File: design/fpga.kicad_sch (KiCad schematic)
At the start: 80 parts, among them J7 DEBUG_FPGA_GPIO, J8 DIGILENT_JTAG_HS2_01X06, SW1 RST, SW2 PROG, U13 XC7S15-FTGB196, U14 IS25LP064A-JKx

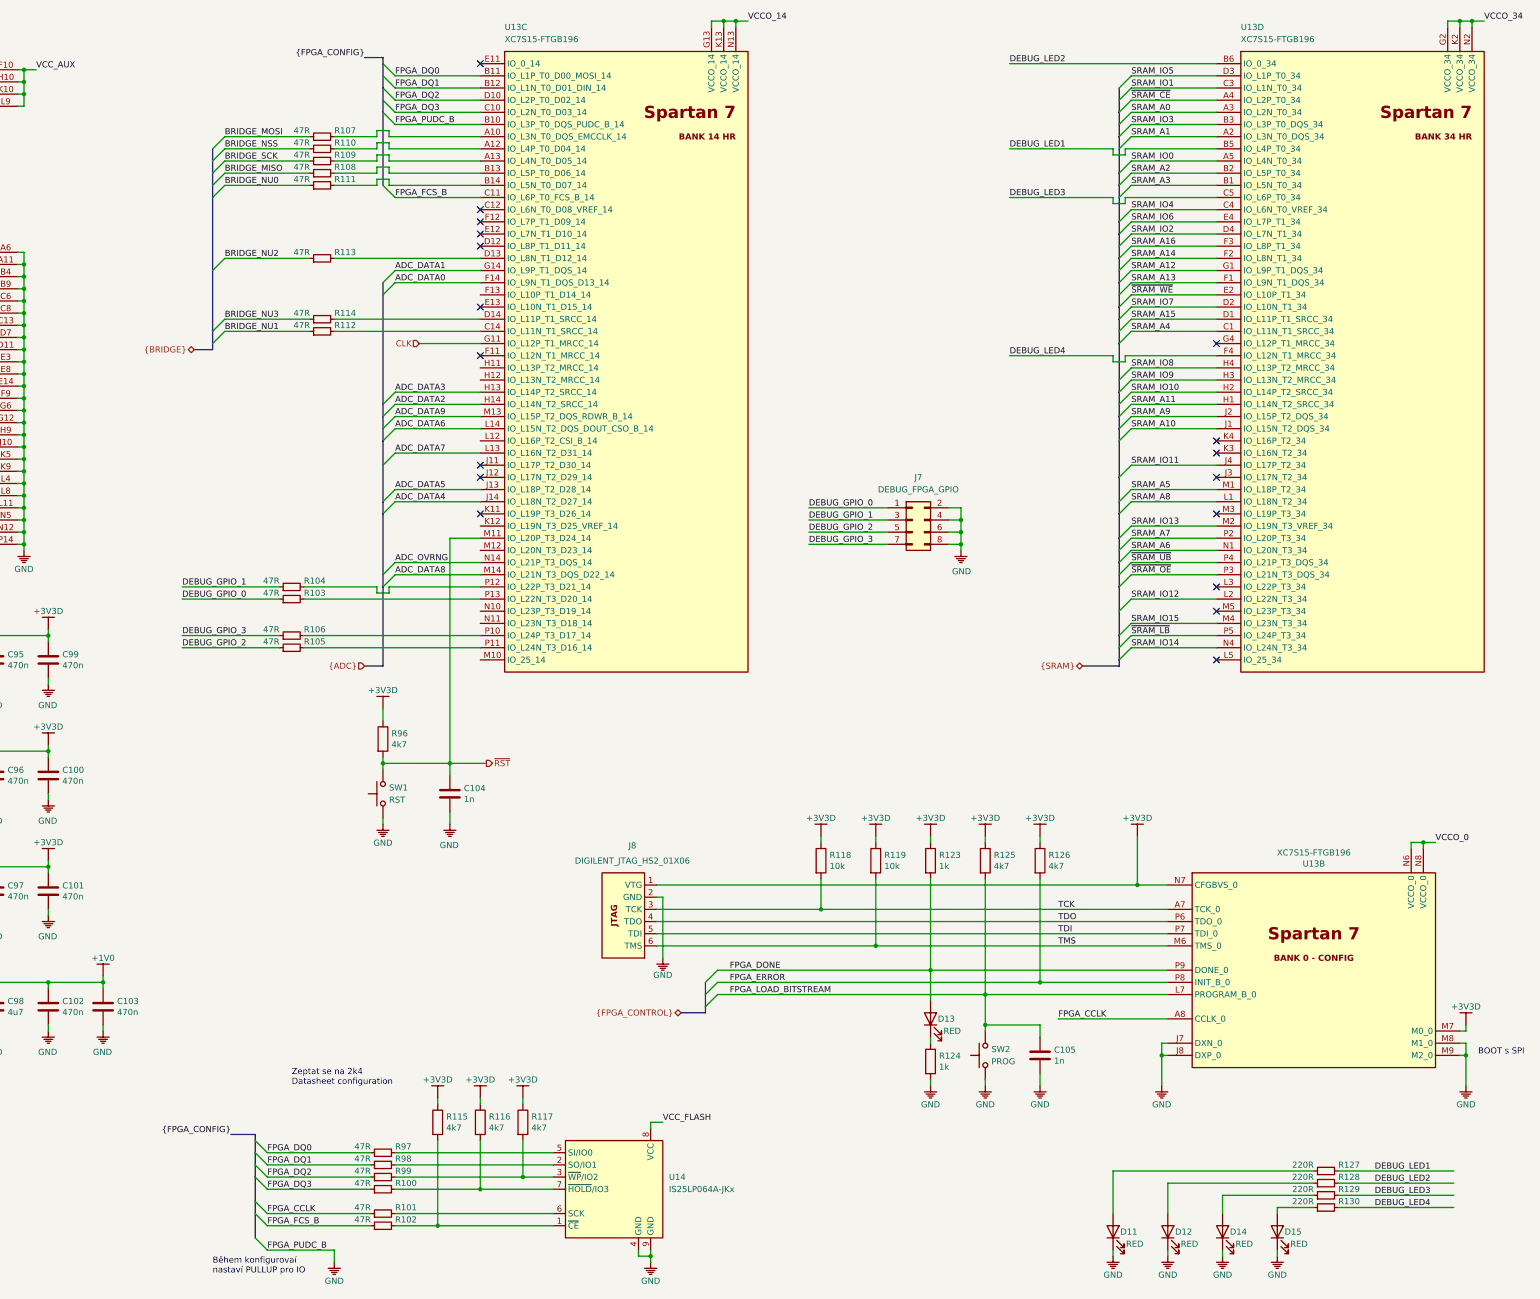
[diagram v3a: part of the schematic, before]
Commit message: Refactored FPGA schematic
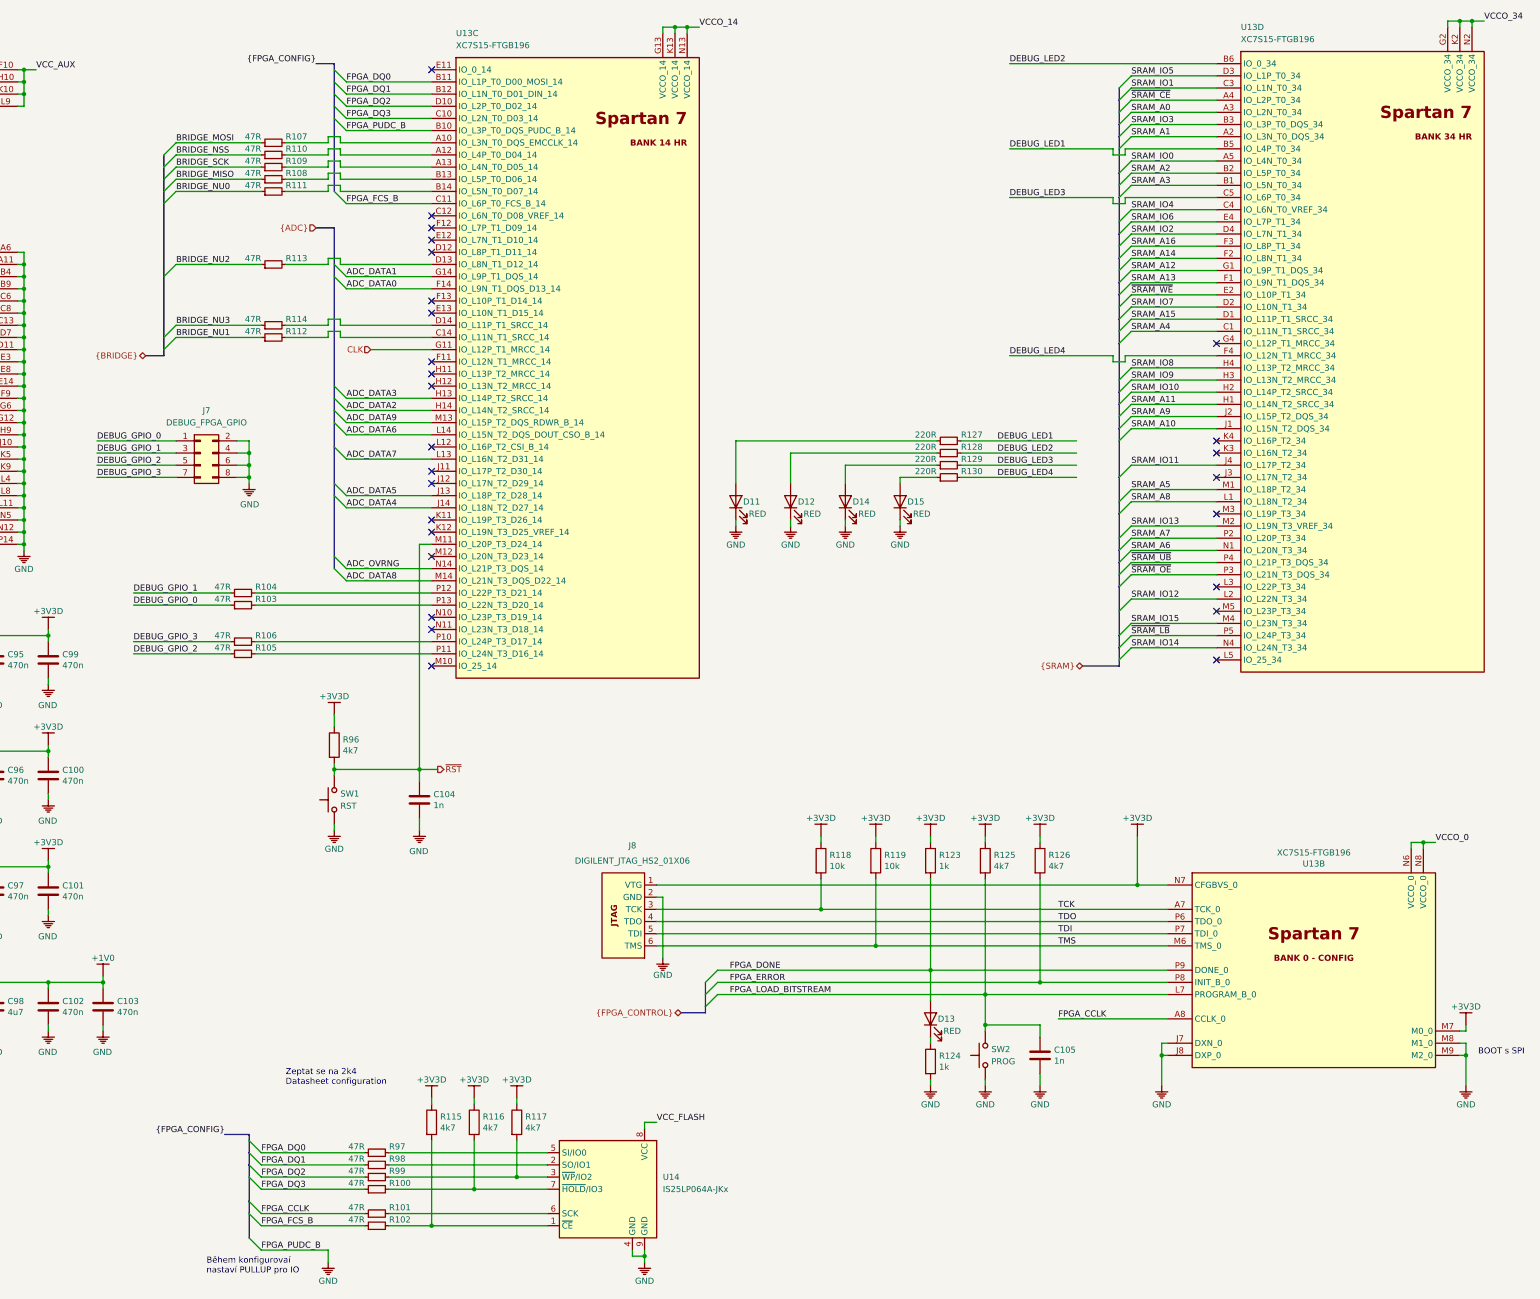
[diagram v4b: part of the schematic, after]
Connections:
- no-connect marks 18 -> 27
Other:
- moved on the sheet: C104, D11, D12, D14, D15, J7, R100, R101, R102, R103, R104, R105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

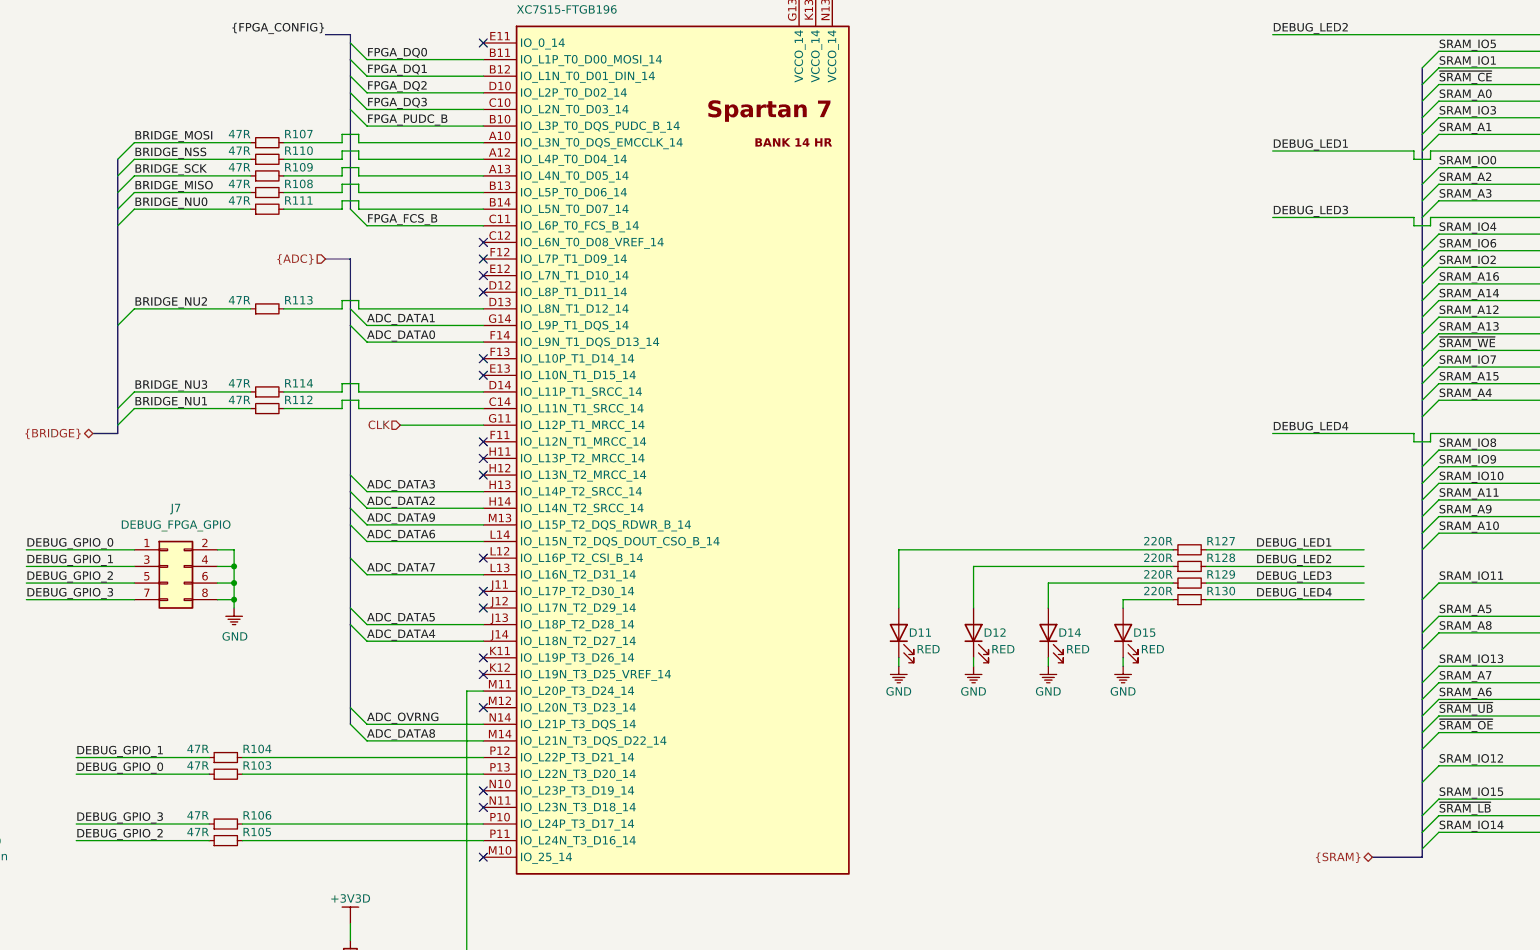
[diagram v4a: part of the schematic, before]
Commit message: Added oscilator layout
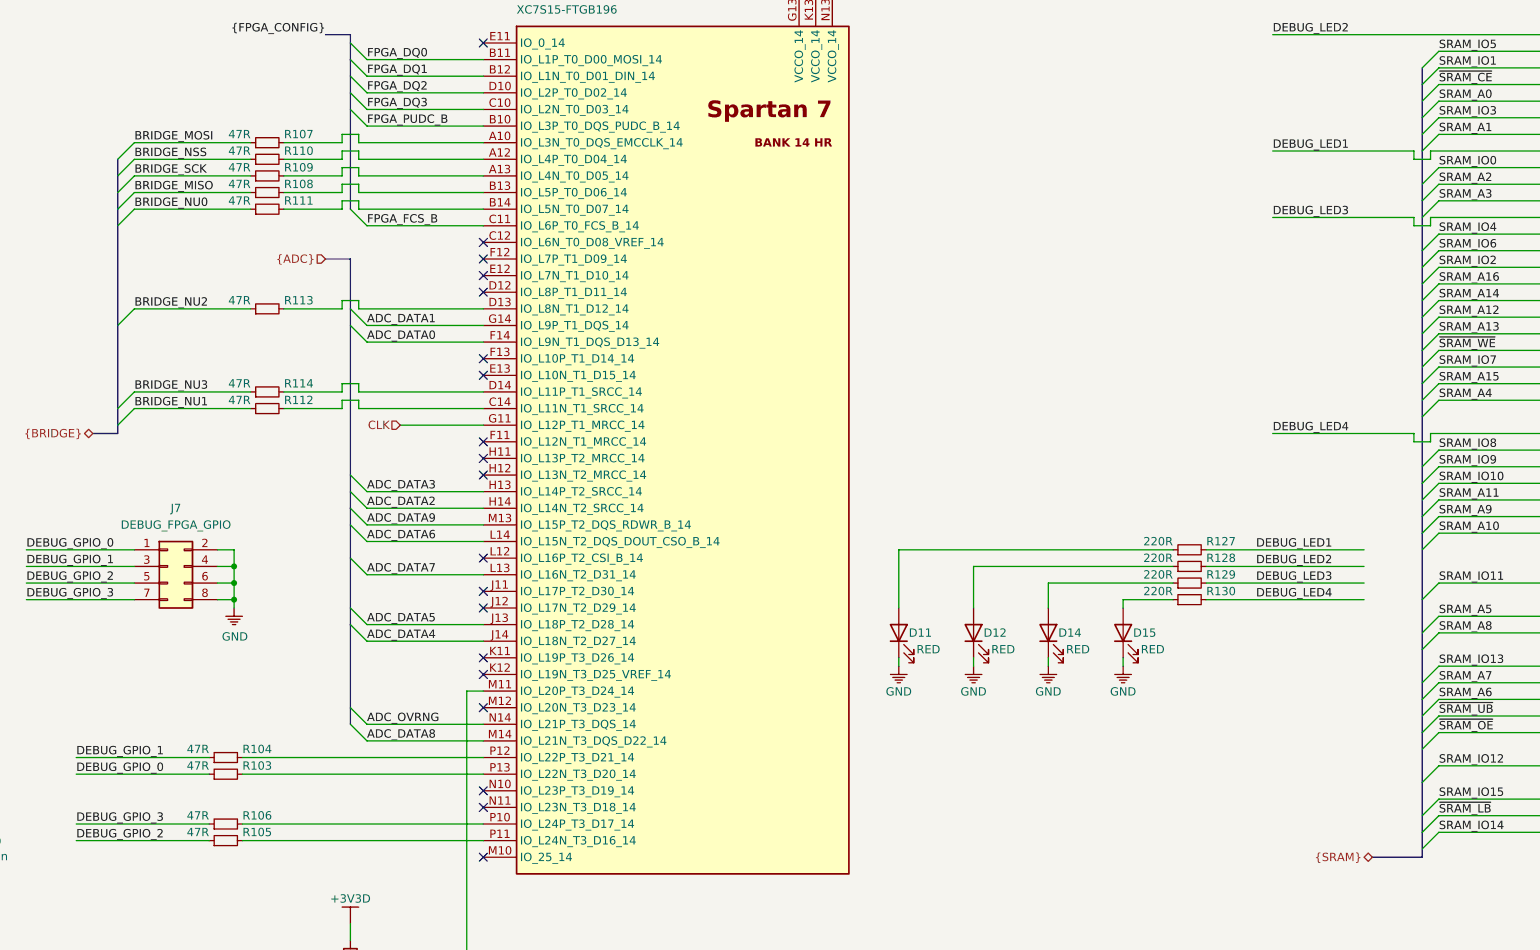
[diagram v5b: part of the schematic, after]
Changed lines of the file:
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@@
-(kicad_sch (version 20200512) (host eeschema "5.99.0-unknown-92ce7ca~101~ubuntu18.04.1")
+(kicad_sch (version 20200512) (host eeschema "5.99.0-unknown-0658d29~101~ubuntu18.04.1")
   (page 8 8)
   (paper "A3")
@@
     (company "Jan Vykydal")
   )
+  (bus_alias "FPGA_CONTROL" (members "FPGA_DONE" "FPGA_ERROR" "FPGA_LOAD_BITSTREAM"))
   (bus_alias "FPGA_CONFIG" (members "FPGA_DQ[0..3]" "FPGA_CCLK" "FPGA_FCS_B" "FPGA_PUDC_B"))
   (bus_alias "BRIDGE" (members "BRIDGE_MOSI" "BRIDGE_MISO" "BRIDGE_SCK" "BRIDGE_NSS" "BRIDGE_NU[0..3]"))
-  (bus_alias "FPGA_CONTROL" (members "FPGA_DONE" "FPGA_ERROR" "FPGA_LOAD_BITSTREAM"))
   (junction (at 26.67 26.67))
   (junction (at 26.67 29.21))
@@
   (junction (at 391.16 232.41))
   (junction (at 392.43 16.51))
-  (no_connect (at 175.26 26.67))
-  (no_connect (at 339.09 104.14))
-  (no_connect (at 339.09 111.76))
-  (no_connect (at 175.26 92.71))
-  (no_connect (at 175.26 110.49))
-  (no_connect (at 339.09 119.38))
-  (no_connect (at 175.26 64.77))
-  (no_connect (at 339.09 106.68))
   (no_connect (at 339.09 134.62))
   (no_connect (at 175.26 87.63))
-  (no_connect (at 175.26 74.93))
+  (no_connect (at 175.26 123.19))
+  (no_connect (at 339.09 106.68))
+  (no_connect (at 175.26 59.69))
+  (no_connect (at 339.09 83.82))
+  (no_connect (at 175.26 113.03))
+  (no_connect (at 175.26 140.97))
+  (no_connect (at 339.09 119.38))
+  (no_connect (at 175.26 26.67))
+  (no_connect (at 175.26 105.41))
+  (no_connect (at 175.26 92.71))
+  (no_connect (at 339.09 111.76))
+  (no_connect (at 175.26 120.65))
+  (no_connect (at 339.09 139.7))
   (no_connect (at 175.26 90.17))
   (no_connect (at 175.26 62.23))
-  (no_connect (at 175.26 59.69))
-  (no_connect (at 175.26 120.65))
-  (no_connect (at 339.09 139.7))
+  (no_connect (at 175.26 64.77))
+  (no_connect (at 175.26 143.51))
+  (no_connect (at 339.09 104.14))
   (no_connect (at 175.26 57.15))
   (no_connect (at 175.26 77.47))
-  (no_connect (at 175.26 105.41))
-  (no_connect (at 175.26 123.19))
+  (no_connect (at 339.09 149.86))
+  (no_connect (at 175.26 110.49))
+  (no_connect (at 175.26 151.13))
   (no_connect (at 175.26 128.27))
-  (no_connect (at 175.26 140.97))
-  (no_connect (at 175.26 143.51))
-  (no_connect (at 175.26 151.13))
-  (no_connect (at 339.09 83.82))
-  (no_connect (at 339.09 149.86))
-  (no_connect (at 175.26 113.03))
+  (no_connect (at 175.26 74.93))
   (bus_entry (at 119.38 44.45) (size 2.54 -2.54))
   (bus_entry (at 119.38 46.99) (size 2.54 -2.54))
@@
   (wire (pts (xy 392.43 16.51) (xy 394.97 16.51)))
   (bus (pts (xy 115.57 86.36) (xy 119.38 86.36)))
-  (bus (pts (xy 119.38 44.45) (xy 119.38 49.53)))
-  (bus (pts (xy 119.38 49.53) (xy 119.38 52.07)))
+  (bus (pts (xy 119.38 44.45) (xy 119.38 46.99)))
+  (bus (pts (xy 119.38 46.99) (xy 119.38 52.07)))
   (bus (pts (xy 119.38 52.07) (xy 119.38 69.85)))
-  (bus (pts (xy 119.38 69.85) (xy 119.38 82.55)))
-  (bus (pts (xy 119.38 82.55) (xy 119.38 86.36)))
+  (bus (pts (xy 119.38 69.85) (xy 119.38 85.09)))
+  (bus (pts (xy 119.38 85.09) (xy 119.38 86.36)))
   (bus (pts (xy 132.08 248.92) (xy 137.16 248.92)))
   (bus (pts (xy 137.16 248.92) (xy 137.16 252.73)))
@@
   (bus (pts (xy 154.94 29.21) (xy 154.94 34.29)))
   (bus (pts (xy 154.94 34.29) (xy 154.94 52.07)))
-  (bus (pts (xy 154.94 59.69) (xy 154.94 69.85)))
-  (bus (pts (xy 154.94 69.85) (xy 154.94 95.25)))
-  (bus (pts (xy 154.94 95.25) (xy 154.94 97.79)))
+  (bus (pts (xy 154.94 59.69) (xy 154.94 67.31)))
+  (bus (pts (xy 154.94 67.31) (xy 154.94 92.71)))
+  (bus (pts (xy 154.94 92.71) (xy 154.94 97.79)))
   (bus (pts (xy 154.94 97.79) (xy 154.94 105.41)))
   (bus (pts (xy 154.94 105.41) (xy 154.94 115.57)))
@@
   (bus (pts (xy 318.77 30.48) (xy 318.77 33.02)))
   (bus (pts (xy 318.77 33.02) (xy 318.77 38.1)))
-  (bus (pts (xy 318.77 38.1) (xy 318.77 40.64)))
-  (bus (pts (xy 318.77 40.64) (xy 318.77 48.26)))
-  (bus (pts (xy 318.77 48.26) (xy 318.77 53.34)))
-  (bus (pts (xy 318.77 53.34) (xy 318.77 60.96)))
-  (bus (pts (xy 318.77 60.96) (xy 318.77 66.04)))
-  (bus (pts (xy 318.77 66.04) (xy 318.77 71.12)))
-  (bus (pts (xy 318.77 71.12) (xy 318.77 73.66)))
+  (bus (pts (xy 318.77 38.1) (xy 318.77 43.18)))
+  (bus (pts (xy 318.77 43.18) (xy 318.77 50.8)))
+  (bus (pts (xy 318.77 50.8) (xy 318.77 58.42)))
+  (bus (pts (xy 318.77 58.42) (xy 318.77 63.5)))
+  (bus (pts (xy 318.77 63.5) (xy 318.77 68.58)))
+  (bus (pts (xy 318.77 68.58) (xy 318.77 73.66)))
   (bus (pts (xy 318.77 73.66) (xy 318.77 78.74)))
   (bus (pts (xy 318.77 78.74) (xy 318.77 83.82)))
   (bus (pts (xy 318.77 83.82) (xy 318.77 93.98)))
-  (bus (pts (xy 318.77 93.98) (xy 318.77 96.52)))
-  (bus (pts (xy 318.77 96.52) (xy 318.77 101.6)))
+  (bus (pts (xy 318.77 93.98) (xy 318.77 99.06)))
+  (bus (pts (xy 318.77 99.06) (xy 318.77 101.6)))
   (bus (pts (xy 318.77 101.6) (xy 318.77 111.76)))
   (bus (pts (xy 318.77 111.76) (xy 318.77 119.38)))
   (bus (pts (xy 318.77 119.38) (xy 318.77 127)))
-  (bus (pts (xy 318.77 127) (xy 318.77 129.54)))
-  (bus (pts (xy 318.77 129.54) (xy 318.77 134.62)))
-  (bus (pts (xy 318.77 134.62) (xy 318.77 144.78)))
-  (bus (pts (xy 318.77 144.78) (xy 318.77 147.32)))
+  (bus (pts (xy 318.77 127) (xy 318.77 132.08)))
+  (bus (pts (xy 318.77 132.08) (xy 318.77 139.7)))
+  (bus (pts (xy 318.77 139.7) (xy 318.77 147.32)))
   (bus (pts (xy 318.77 147.32) (xy 318.77 151.13)))
   (bus (pts (xy 318.77 151.13) (xy 311.15 151.13)))
